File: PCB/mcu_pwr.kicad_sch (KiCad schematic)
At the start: 26 parts, among them J1 Conn_01x06, J4 Conn_01x03, SW1 SW_Push, SW2 SW_Push, U1 ESP32-WROOM-32, U6 TLV75533PDBV

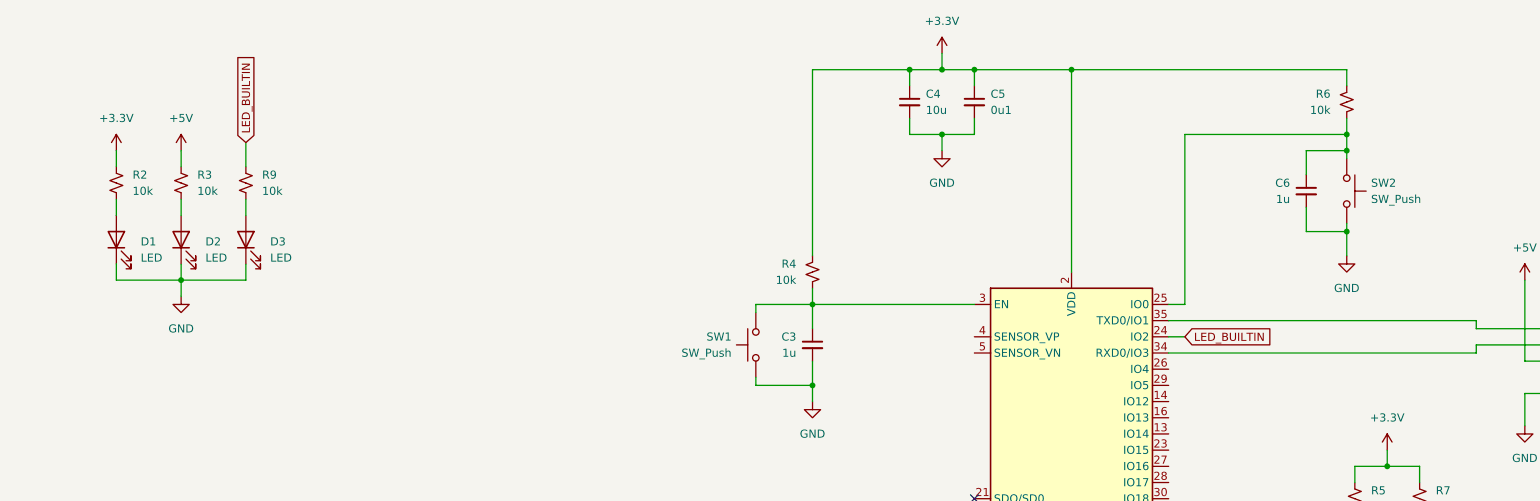
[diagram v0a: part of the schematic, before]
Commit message: Moved kicad files to the PCB folder
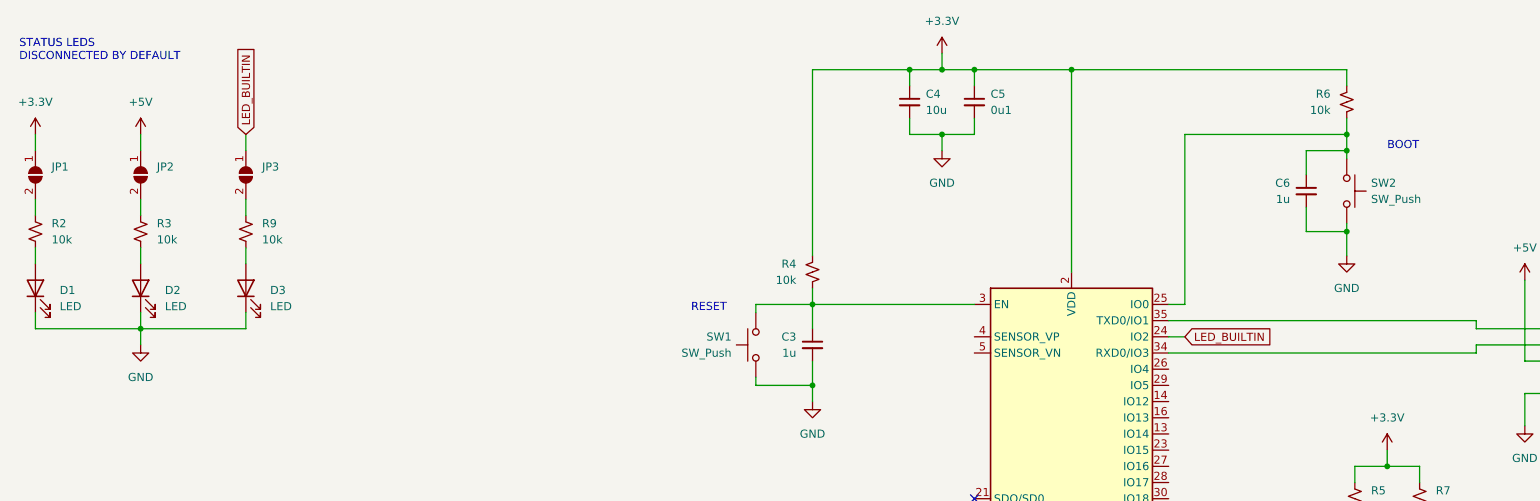
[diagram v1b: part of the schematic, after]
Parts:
- added JP1, JP2, JP3: (no value), symbol Jumper:SolderJumper_2_Open
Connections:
- net +3.3V: now also JP1.1 (A); no longer R2.1
- net +5V: now also JP2.1 (A); no longer R3.1
- net LED_BUILTIN: now also JP3.1 (A); no longer R9.1
- new net: JP2.2 (B), R3.1
- new net: JP3.2 (B), R9.1
- new net: JP1.2 (B), R2.1
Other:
- note added: "BOOT"
- note added: "RESET"
- note added: "STATUS LEDS DISCONNECTED BY DEFAULT"
- moved on the sheet: D1, D2, D3, R2, R3, R9

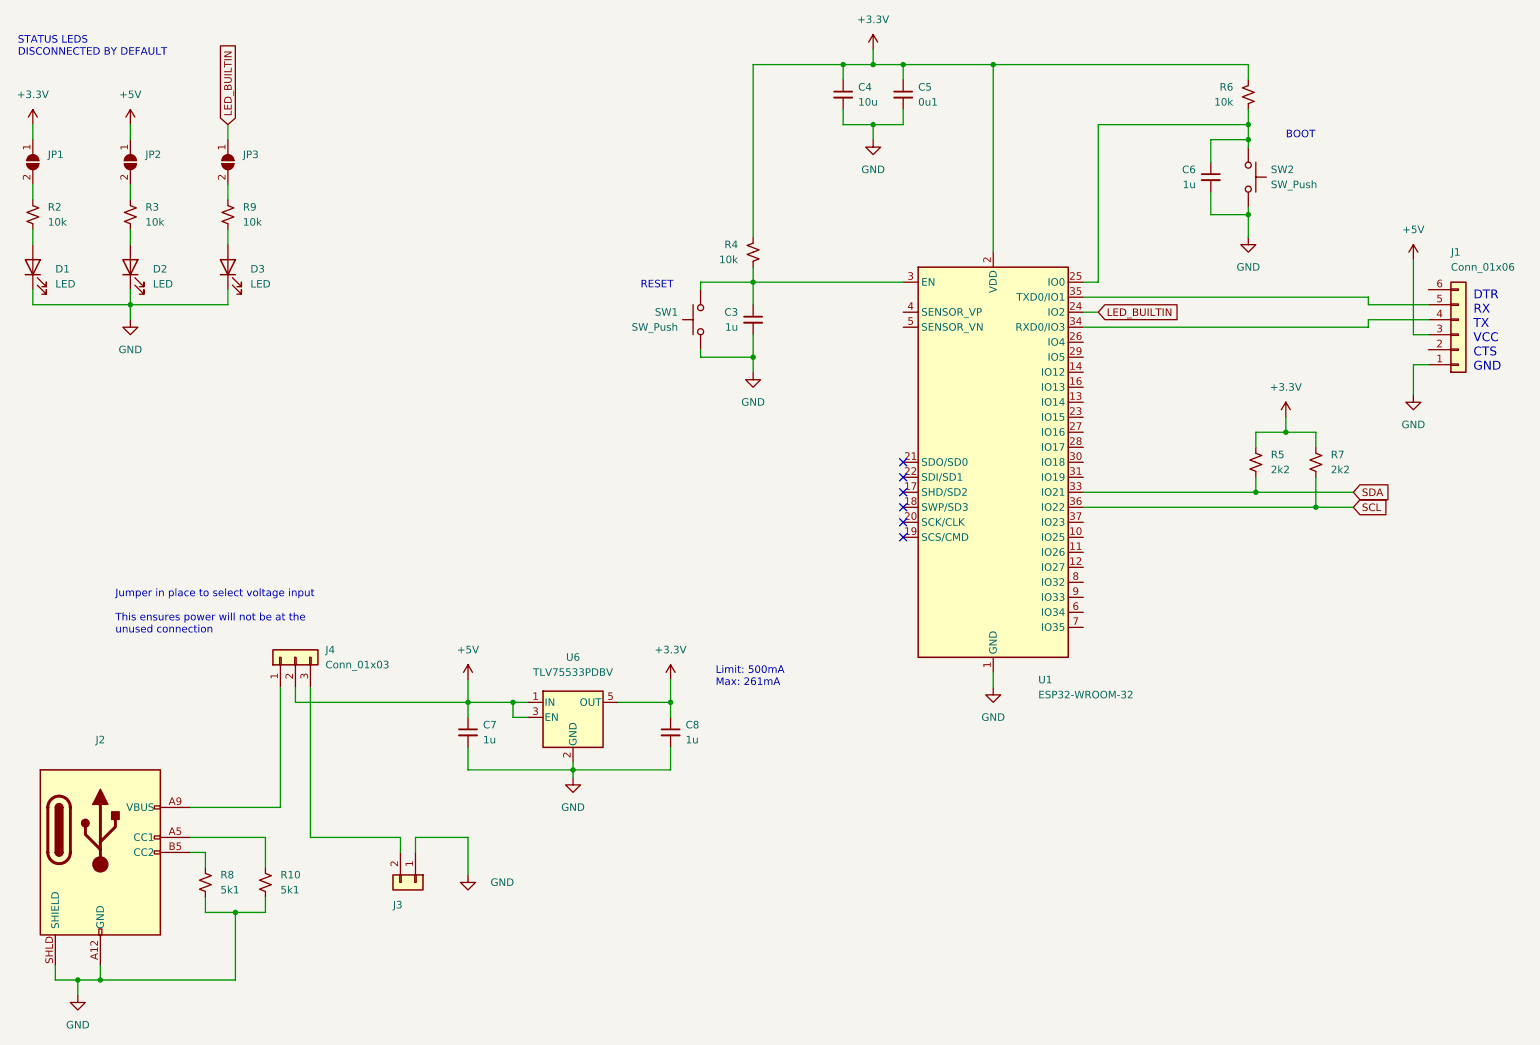
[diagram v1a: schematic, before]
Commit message: updated footprints and started board layout
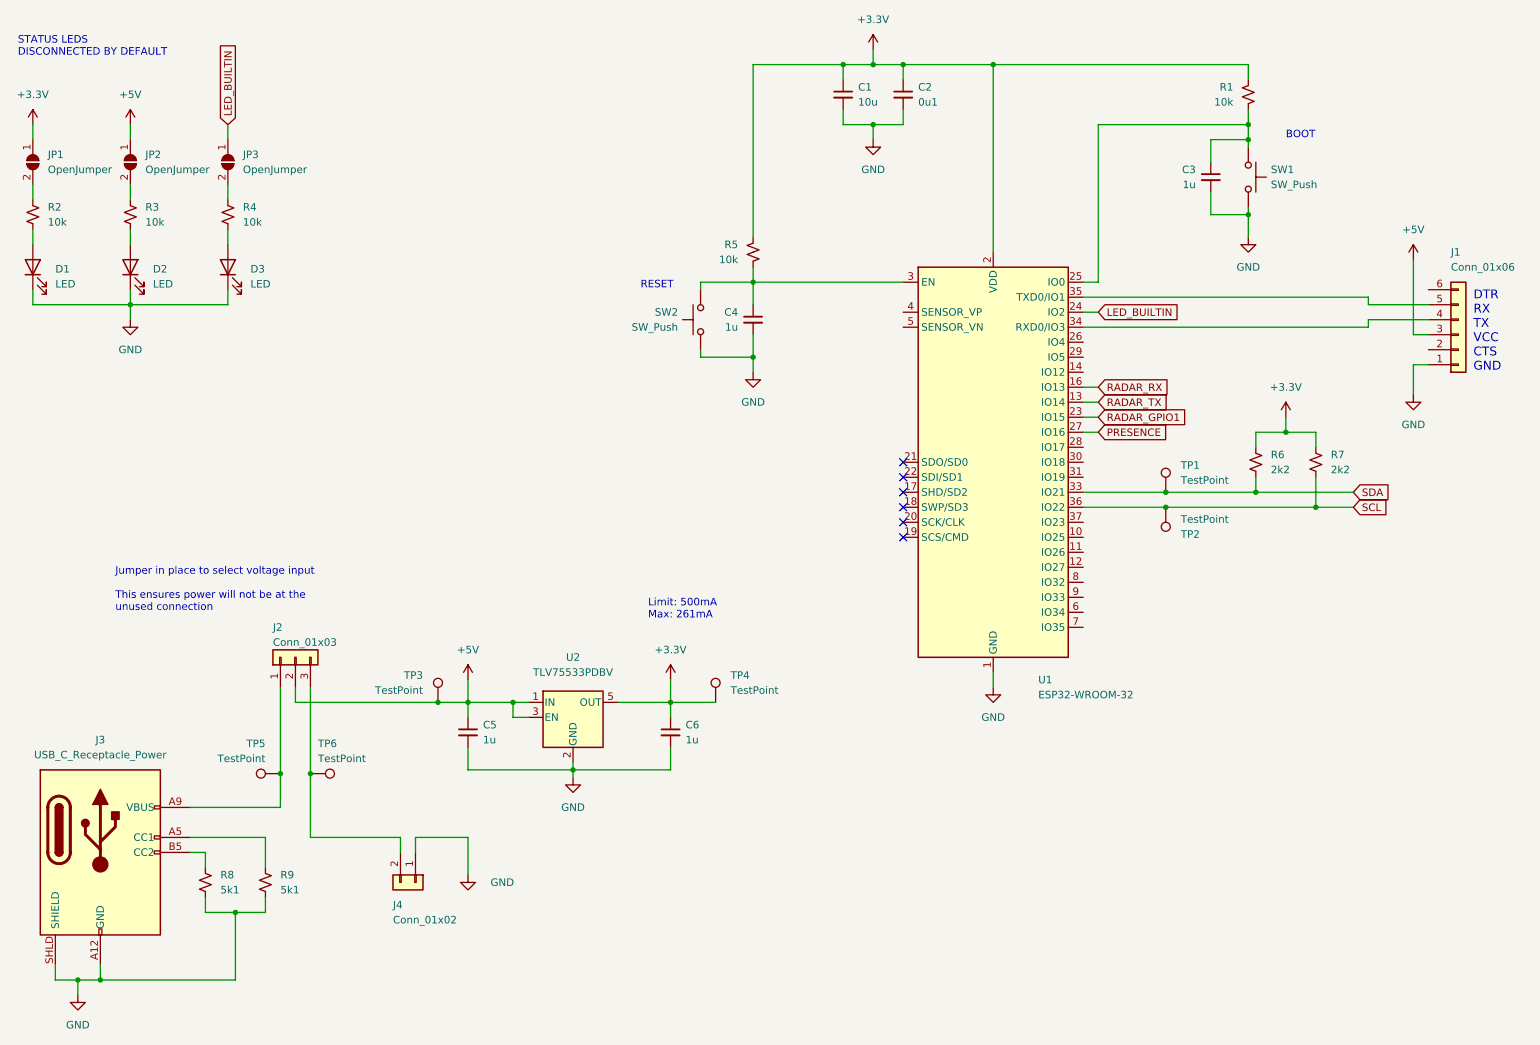
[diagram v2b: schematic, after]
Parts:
- added TP1, TP2, TP3, TP4, TP5, TP6: TestPoint, symbol Connector:TestPoint
- J3: renamed from J2; value (none) -> USB_C_Receptacle_Power; footprint (none) -> My Footprints:USB_C_Power
- J4: renamed from J3; value (none) -> Conn_01x02; footprint (none) -> Connector_PinHeader_2.54mm:PinHeader_1x02_P2.54mm_Vertical
- JP1, JP2, JP3: value (none) -> OpenJumper; footprint (none) -> Jumper:SolderJumper-2_P1.3mm_Open_TrianglePad1.0x1.5mm
- renumbered C4 to C1, C5 to C2, C6 to C3, C3 to C4, C7 to C5, C8 to C6, J4 to J2, R6 to R1, R9 to R4, R4 to R5, R5 to R6, R10 to R9, SW2 to SW1, SW1 to SW2, U6 to U2
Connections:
- net +3.3V: now also TP4.1
- net +5V: now also TP3.1
- net SCL: now also TP2.1
- net SDA: now also TP1.1
- net RADAR_TX: now reaches U1.13 (IO14)
- net RADAR_RX: now reaches U1.16 (IO13)
- net RADAR_GPIO1: now reaches U1.23 (IO15)
- net PRESENCE: now reaches U1.27 (IO16)
- net at J2.1 (Pin_1), J3.A9 (VBUS), J3.B9 (VBUS): now also TP5.1
- net at J2.3 (Pin_3), J4.2 (Pin_2): now also TP6.1

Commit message: board layout work
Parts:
- removed TP5, TP6: TestPoint, symbol Connector:TestPoint
- TP1, TP2, TP3, TP4: footprint (none) -> TestPoint:TestPoint_THTPad_2.0x2.0mm_Drill1.0mm
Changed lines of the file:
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@@
   (junction (at 228.6 48.26) (diameter 0) (color 0 0 0 0)
-  )
-  (junction (at 69.85 142.875) (diameter 0) (color 0 0 0 0)
-  )
-  (junction (at 64.77 142.875) (diameter 0) (color 0 0 0 0)
   )
   (junction (at 96.52 130.81) (diameter 0) (color 0 0 0 0)
@@
     (stroke (width 0) (type default) (color 0 0 0 0))
   )
-  (wire (pts (xy 64.77 128.27) (xy 64.77 142.875))
-    (stroke (width 0) (type default) (color 0 0 0 0))
-  )
   (wire (pts (xy 256.54 73.66) (xy 259.08 73.66))
     (stroke (width 0) (type default) (color 0 0 0 0))
@@
     (stroke (width 0) (type default) (color 0 0 0 0))
   )
-  (wire (pts (xy 64.77 142.875) (xy 64.77 148.59))
+  (wire (pts (xy 64.77 128.27) (xy 64.77 148.59))
     (stroke (width 0) (type default) (color 0 0 0 0))
   )
@@
     (stroke (width 0) (type default) (color 0 0 0 0))
   )
-  (wire (pts (xy 69.85 128.27) (xy 69.85 142.875))
+  (wire (pts (xy 69.85 128.27) (xy 69.85 153.67))
     (stroke (width 0) (type default) (color 0 0 0 0))
   )
@@
   )
   (wire (pts (xy 39.37 63.5) (xy 39.37 66.04))
-    (stroke (width 0) (type default) (color 0 0 0 0))
-  )
-  (wire (pts (xy 69.85 142.875) (xy 69.85 153.67))
     (stroke (width 0) (type default) (color 0 0 0 0))
   )
@@
       (effects (font (size 1.27 1.27)) (justify left))
     )
-    (property "Footprint" "" (id 2) (at 219.71 95.25 0)
+    (property "Footprint" "TestPoint:TestPoint_THTPad_2.0x2.0mm_Drill1.0mm" (id 2) (at 219.71 95.25 0)
       (effects (font (size 1.27 1.27)) hide)
     )
@@
       (effects (font (size 1.27 1.27)) (justify left))
     )
-    (property "Footprint" "" (id 2) (at 219.71 97.79 0)
+    (property "Footprint" "TestPoint:TestPoint_THTPad_2.0x2.0mm_Drill1.0mm" (id 2) (at 219.71 97.79 0)
       (effects (font (size 1.27 1.27)) hide)
     )
@@
       (effects (font (size 1.27 1.27)) (justify left))
     )
-    (property "Footprint" "" (id 2) (at 143.51 130.81 0)
+    (property "Footprint" "TestPoint:TestPoint_THTPad_2.0x2.0mm_Drill1.0mm" (id 2) (at 143.51 130.81 0)
       (effects (font (size 1.27 1.27)) hide)
     )
@@
       (effects (font (size 1.27 1.27)) (justify left))
     )
-    (property "Footprint" "" (id 2) (at 86.36 130.81 0)
+    (property "Footprint" "TestPoint:TestPoint_THTPad_2.0x2.0mm_Drill1.0mm" (id 2) (at 86.36 130.81 0)
       (effects (font (size 1.27 1.27)) hide)
     )
@@
     (pin "1")
   )
-  (symbol (lib_id "Connector:TestPoint") (at 69.85 142.875 270) (unit 1)
-    (in_bom yes) (on_board yes)
-    (property "Reference" "TP6" (id 0) (at 71.12 137.795 90)
-      (effects (font (size 1.27 1.27)) (justify left))
-    )
-    (property "Value" "TestPoint" (id 1) (at 71.12 140.335 90)
-      (effects (font (size 1.27 1.27)) (justify left))
-    )
-    (property "Footprint" "" (id 2) (at 69.85 147.955 0)
-      (effects (font (size 1.27 1.27)) hide)
-    )
-    (property "Datasheet" "~" (id 3) (at 69.85 147.955 0)
-      (effects (font (size 1.27 1.27)) hide)
-    )
-    (pin "1")
-  )
   (symbol (lib_id "Device:C_Small") (at 222.25 41.91 0) (mirror y) (unit 1)
     (in_bom yes) (on_board yes) (fields_autoplaced)
@@
     (pin "2")
   )
-  (symbol (lib_id "Connector:TestPoint") (at 64.77 142.875 90) (unit 1)
-    (in_bom yes) (on_board yes)
-    (property "Reference" "TP5" (id 0) (at 62.23 137.795 90)
-      (effects (font (size 1.27 1.27)) (justify left))
-    )
-    (property "Value" "TestPoint" (id 1) (at 62.23 140.335 90)
-      (effects (font (size 1.27 1.27)) (justify left))
-    )
-    (property "Footprint" "" (id 2) (at 64.77 137.795 0)
-      (effects (font (size 1.27 1.27)) hide)
-    )
-    (property "Datasheet" "~" (id 3) (at 64.77 137.795 0)
-      (effects (font (size 1.27 1.27)) hide)
-    )
-    (pin "1")
-  )
   (symbol (lib_id "power:GND") (at 165.1 35.56 0) (unit 1)
